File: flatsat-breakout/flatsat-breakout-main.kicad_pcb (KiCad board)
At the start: 2 copper layers, 34 x 94 mm, 10 parts, among them J1 SFM-120-02-L-DH-TR, J2 61204021621, J3 61204021621, J4 68000-227HLF, J5 Conn_02x08_Odd_Even

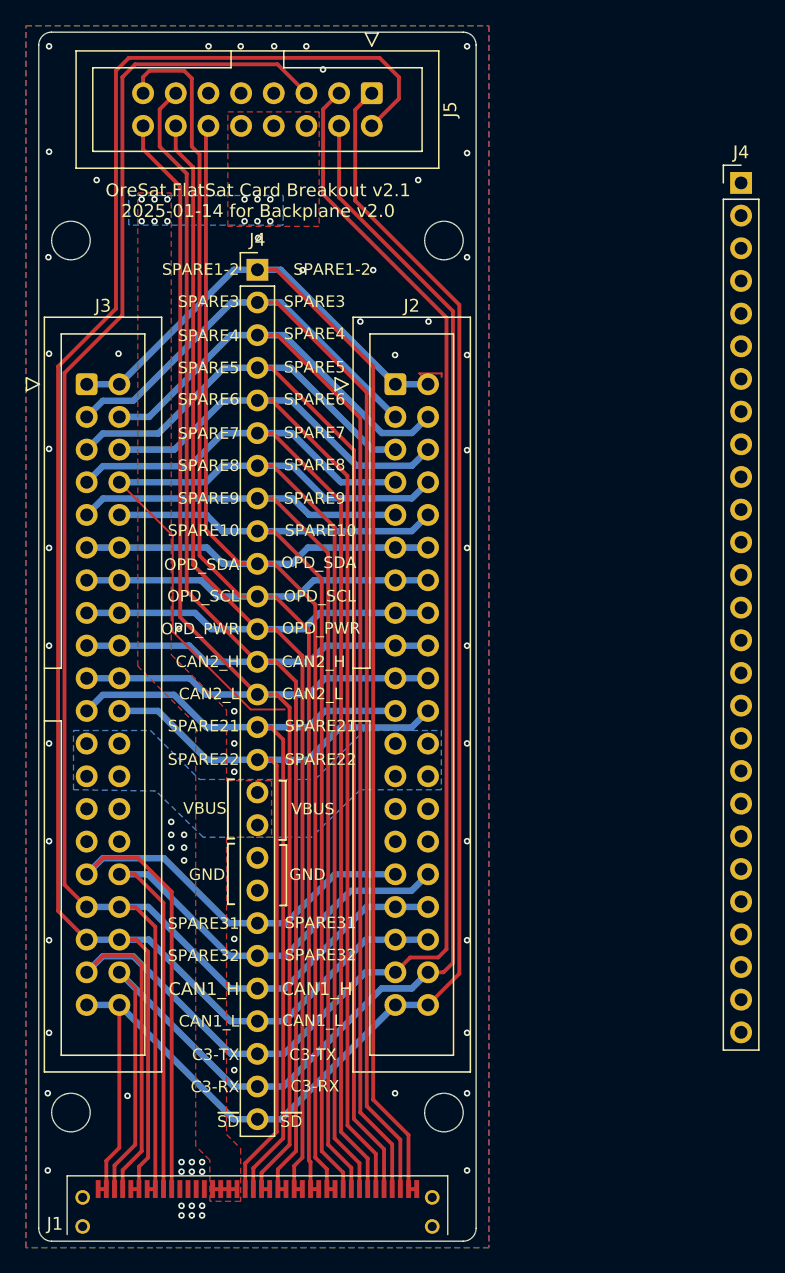
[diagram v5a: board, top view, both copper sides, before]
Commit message: Update flatsat-breakout pcb
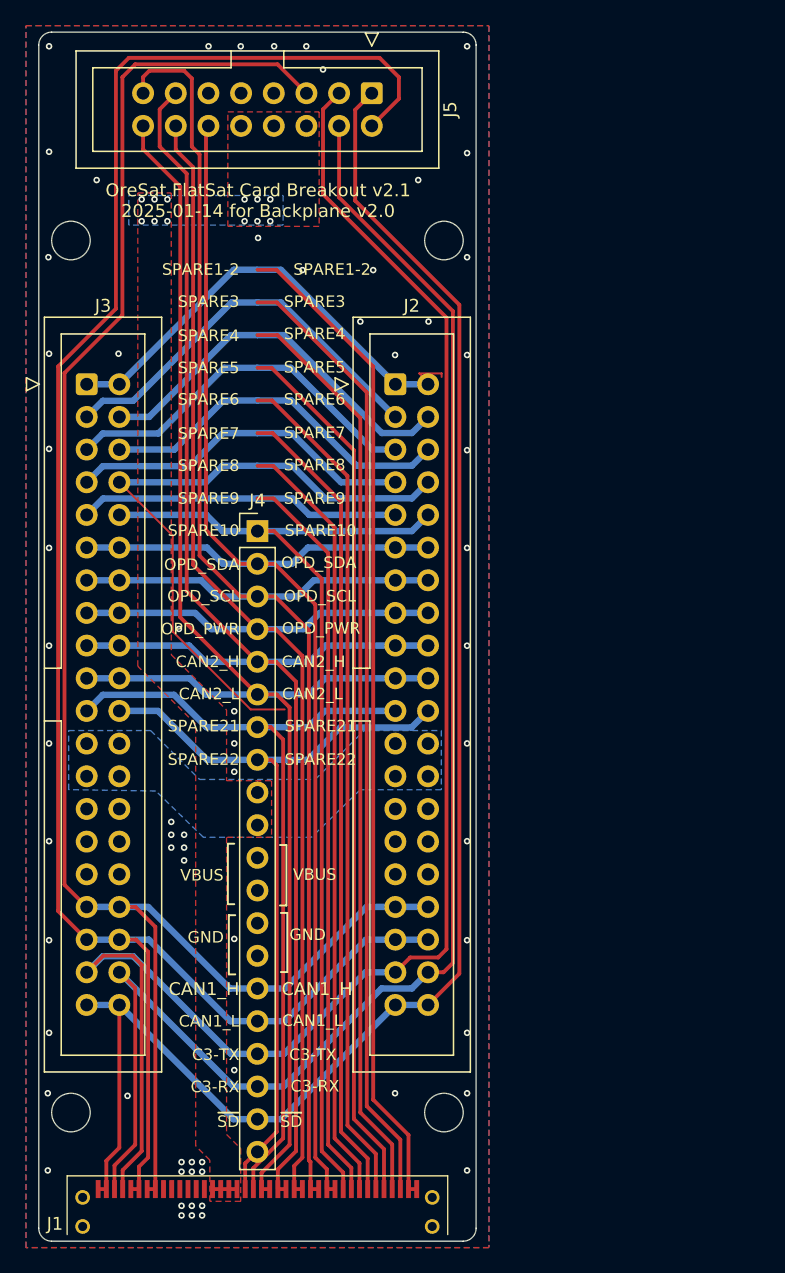
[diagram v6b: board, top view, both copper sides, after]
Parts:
- removed the J4 at (187.6, 60.2)
- J4: footprint Connector_PinHeader_2.54mm:PinHeader_1x27_P2.54mm_Vertical -> Connector_PinHeader_2.54mm:PinHeader_1x20_P2.54mm_Vertical
- moved J4 20.3 mm to (150.0, 87.3)
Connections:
- J4 pad 1: /SPARE1 -> /MAG-SDA
- J4 pad 10: OPD_SDA -> CAN2_L
- J4 pad 11: OPD_SCL -> VBUS
- J4 pad 12: OPD_PWR -> VBUS
- J4 pad 13: CAN2_H -> GND
- J4 pad 14: CAN2_L -> GND
- J4 pad 15: /SPARE21 -> CAN1_H
- J4 pad 16: /SPARE22 -> CAN1_L
- J4 pad 17: VBUS -> C3-UART-TX
- J4 pad 18: VBUS -> C3-UART-RX
- J4 pad 19: GND -> ~{SD}
- J4 pad 2: /SPARE3 -> /MAG-SCL
- J4 pad 3: /SPARE4 -> /MAG-POWER
- J4 pad 4: /SPARE5 -> /HELICAL-DEPLOY
- J4 pad 5: /SPARE6 -> /TURNSTILE-DEPLOY
- J4 pad 6: /SPARE7 -> OPD_SDA
- J4 pad 7: /SPARE8 -> OPD_SCL
- J4 pad 8: /SPARE9 -> OPD_PWR
- J4 pad 9: /SPARE10 -> CAN2_H
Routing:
- net /MAG-SCL: track 0.00 -> 207.7 mm
- net /MAG-POWER: track 0.00 -> 191.8 mm
- net /HELICAL-DEPLOY: track 24.5 -> 201.0 mm
- net /SPARE1: track 111.8 -> 0.00 mm
- net /MAG-SDA: track 3.14 -> 114.9 mm
- net /SPARE3: track 105.8 -> 0.00 mm
- net /SPARE4: track 102.0 -> 0.00 mm
- net /SPARE5: track 97.8 -> 0.00 mm
- net /SPARE6: track 94.0 -> 0.00 mm
- net /SPARE7: track 90.2 -> 0.00 mm
- net /SPARE8: track 86.3 -> 0.00 mm
- net /TURNSTILE-DEPLOY: track 0.00 -> 82.5 mm
- net /SPARE9: track 82.5 -> 0.00 mm
- net /SPARE10: track 79.7 -> 0.00 mm
- net (no net): track 0.00 -> 79.7 mm
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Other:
- board text removed: "SPARE31"
- board text removed: "SPARE32"

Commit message: Traces for front layer
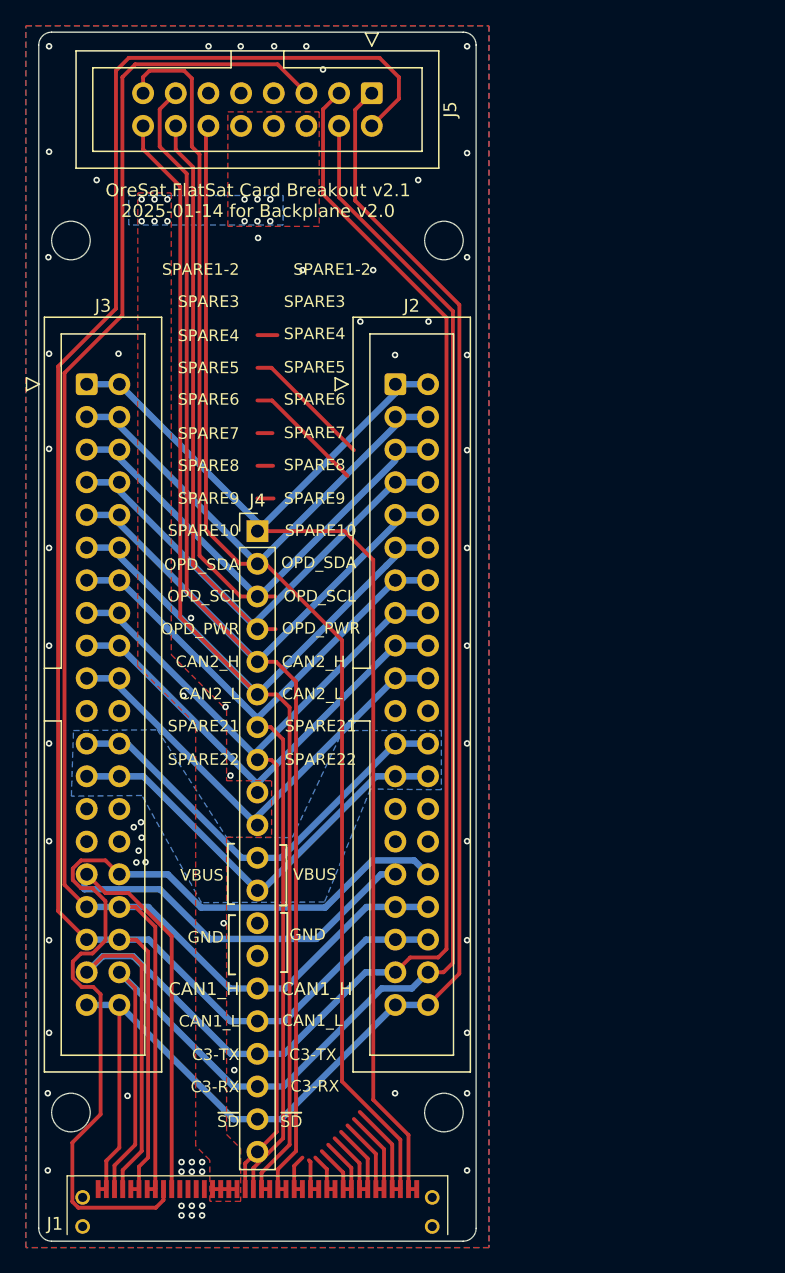
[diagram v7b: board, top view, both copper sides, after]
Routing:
- net /HELICAL-DEPLOY: track 201.0 -> 49.5 mm
- net /MAG-POWER: track 191.8 -> 69.0 mm
- net /MAG-SCL: track 207.7 -> 99.0 mm
- net (no net): track 79.7 -> 0.00 mm
- net /SPARE32: track 0.00 -> 71.2 mm
- net VBUS: track 1.91 -> 70.4 mm
- net /SPARE31: track 0.00 -> 58.1 mm
- net OPD_SDA: track 116.4 -> 76.8 mm
- net /TURNSTILE-DEPLOY: track 82.5 -> 46.5 mm
- net OPD_SCL: track 125.5 -> 91.1 mm
- net OPD_PWR: track 116.1 -> 83.0 mm
- net /SPARE22: track 62.8 -> 35.6 mm
- net /SPARE21: track 64.4 -> 38.3 mm
- net /MAG-SDA: track 114.9 -> 97.6 mm
- net CAN2_H: track 119.8 -> 129.3 mm
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
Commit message: added more traces to front layer
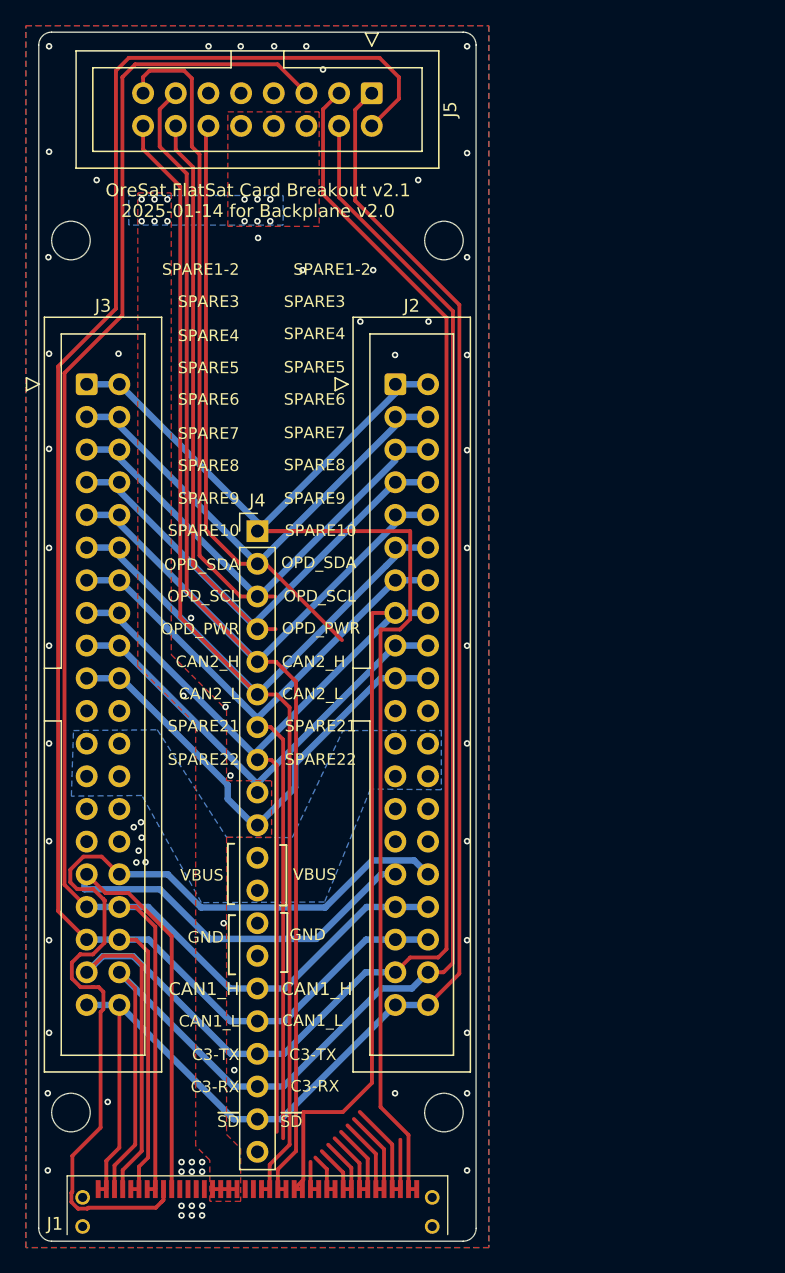
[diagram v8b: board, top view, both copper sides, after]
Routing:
- net OPD_PWR: track 83.0 -> 161.4 mm
- net VBUS: track 70.4 -> 2.58 mm
- net /MAG-SCL: track 99.0 -> 56.8 mm
- net /SPARE21: track 38.3 -> 0.00 mm
- net /SPARE22: track 35.6 -> 0.00 mm
- net OPD_SCL: track 91.1 -> 124.3 mm
- net /MAG-POWER: track 69.0 -> 49.4 mm
- net /MAG-SDA: track 97.6 -> 110.1 mm
- net /HELICAL-DEPLOY: track 49.5 -> 47.1 mm
- net CAN2_L: track 126.2 -> 127.9 mm
- net /SPARE32: track 71.2 -> 72.7 mm
- net /TURNSTILE-DEPLOY: track 46.5 -> 45.2 mm
